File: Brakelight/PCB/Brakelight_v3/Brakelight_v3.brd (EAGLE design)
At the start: 61.1 x 55.9 mm, 57 parts, among them U1 LM358MX

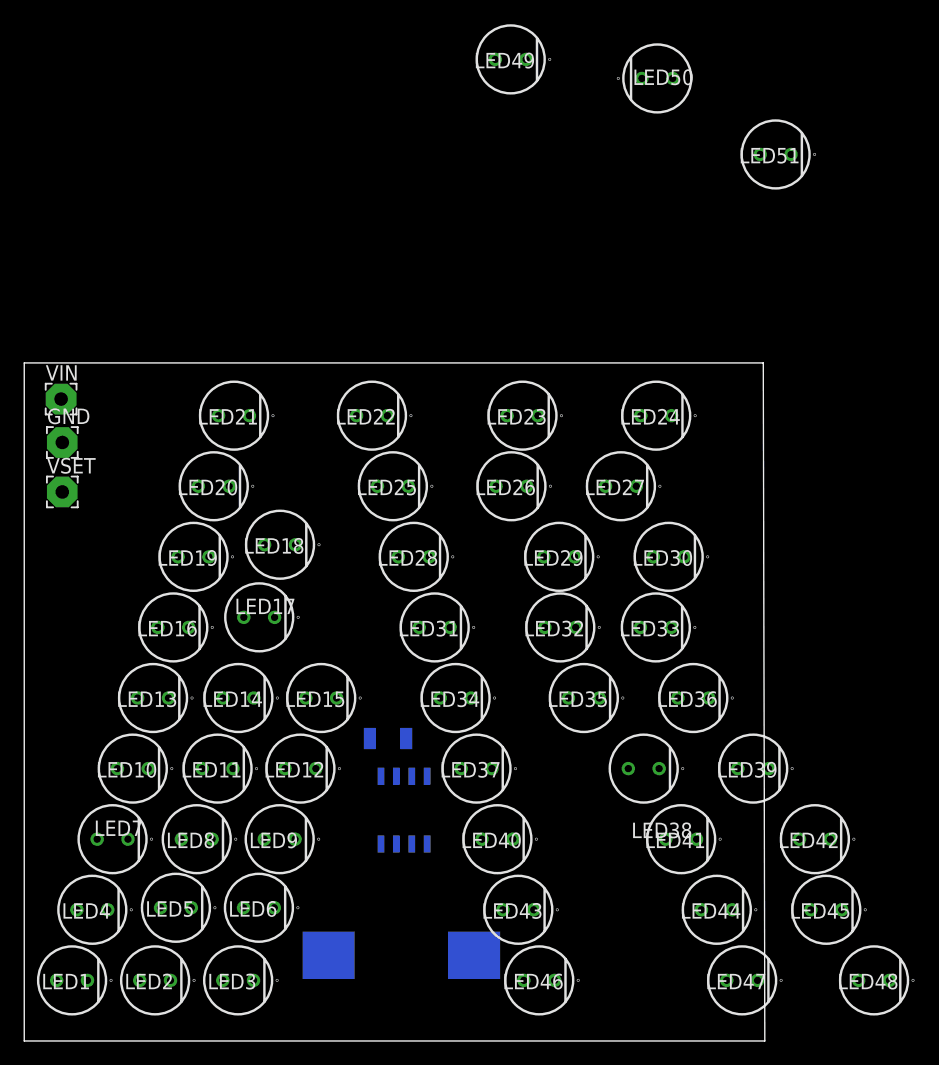
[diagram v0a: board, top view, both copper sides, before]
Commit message: Brakelight - Fixed positions ready for tracing
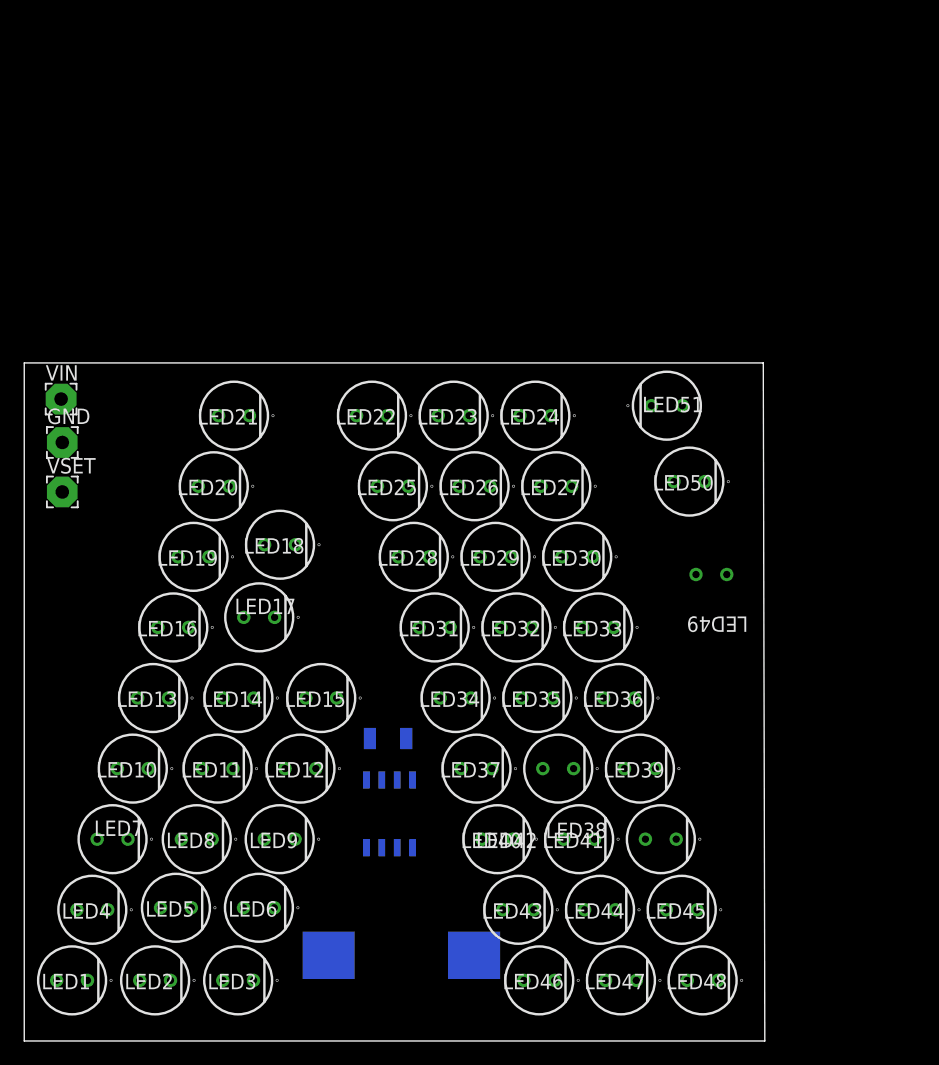
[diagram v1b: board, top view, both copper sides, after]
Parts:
- moved LED49 45.6 mm to (56.5, 36.0), flipped to the bottom
- moved LED50 33.4 mm to (54.7, 43.6), turned to 0 degrees
- moved LED51 22.6 mm to (52.9, 49.9), turned to 180 degrees
- moved LED48 14.1 mm to (55.8, 2.50)
- moved LED42 12.7 mm to (52.4, 14.1)
- moved LED45 11.9 mm to (54.1, 8.32)
- moved LED47 10.00 mm to (49.1, 2.50)
- moved LED24 9.97 mm to (42.0, 49.1)
- moved LED44 9.63 mm to (47.3, 8.32)
- moved LED39 9.34 mm to (50.6, 20.0)
- moved LED41 8.42 mm to (45.6, 14.1)
- moved LED30 7.55 mm to (45.5, 37.4)
- moved LED38 7.05 mm to (43.9, 20.0)
- moved LED36 6.13 mm to (48.9, 25.8)
- moved LED23 5.68 mm to (35.3, 49.1)
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
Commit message: Brakelight only stubs left
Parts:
- moved VIN 40.0 mm to (27.9, 19.2), flipped to the bottom
- moved GND 39.3 mm to (27.9, 16.5), flipped to the bottom
- moved VSET 38.3 mm to (27.9, 13.7), flipped to the bottom
- moved U1 2.16 mm to (32.1, 15.7)
- moved R1 2.00 mm to (31.9, 22.4), turned to 135 degrees
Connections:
- net N$36 renamed LEDK
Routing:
- net LEDK: track 0.00 -> 155.2 mm
- net N$37: track 0.00 -> 19.5 mm
- net N$35: track 0.00 -> 11.3 mm, vias 0 -> 1
- net ISENSE: track 0.00 -> 8.38 mm
- net N$33: track 0.00 -> 7.88 mm
- net N$34: track 0.00 -> 6.53 mm
- net N$12: track 0.00 -> 6.05 mm
- net N$14: track 0.00 -> 5.89 mm
- net N$13: track 0.00 -> 5.89 mm
- net VIN: track 0.00 -> 5.40 mm
- net N$11: track 0.00 -> 4.62 mm
- net N$9: track 0.00 -> 4.50 mm
- net N$7: track 0.00 -> 4.45 mm
- net N$5: track 0.00 -> 4.40 mm
- net N$3: track 0.00 -> 4.36 mm
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- added copper zone on layer 16, net GND
- added copper zone on layer 1, net ISENSE

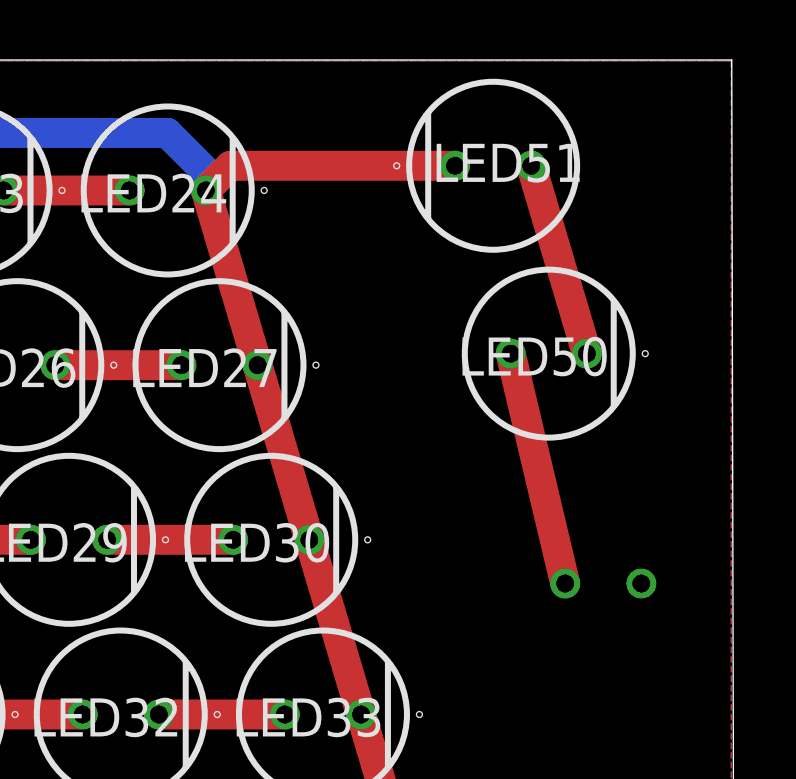
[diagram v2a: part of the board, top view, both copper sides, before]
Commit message: Ready: Brakelight PCB
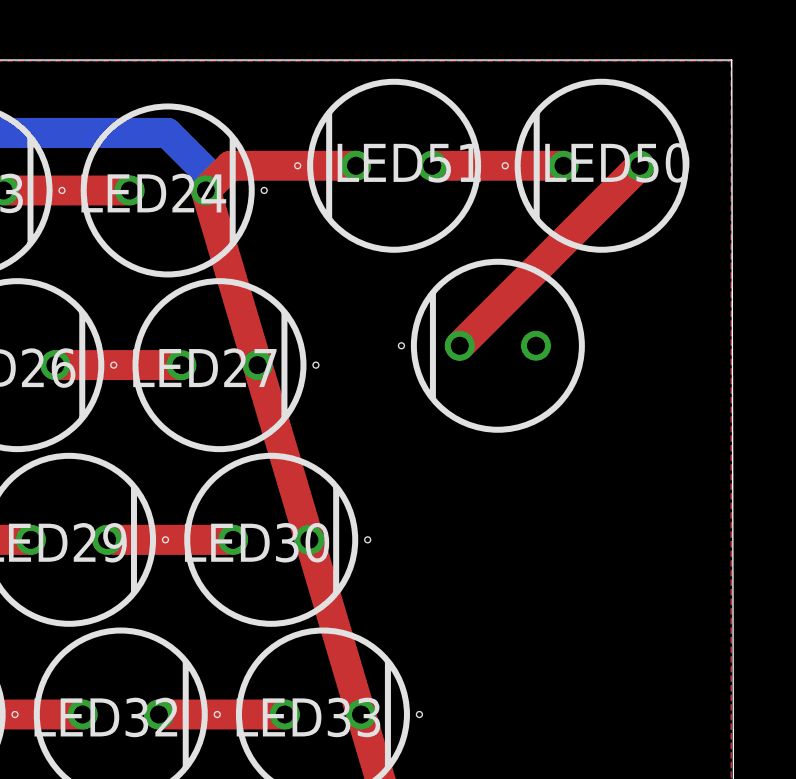
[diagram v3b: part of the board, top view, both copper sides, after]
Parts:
- moved LED49 8.67 mm to (53.0, 43.9), flipped to the top, turned to 180 degrees
- moved LED50 6.50 mm to (56.5, 49.9), turned to 180 degrees
- moved LED51 3.30 mm to (49.6, 49.9)
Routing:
- net LEDK: track 155.2 -> 151.9 mm
- net N$34: track 6.53 -> 4.38 mm
- net N$33: track 7.88 -> 8.48 mm
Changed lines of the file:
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@@
 <?xml version="1.0" encoding="utf-8"?>
 <!DOCTYPE eagle SYSTEM "eagle.dtd">
-<eagle version="9.2.2">
+<eagle version="9.2.1">
 <drawing>
 <settings>
@@
 <attribute name="VALUE" x="55.31395" y="2.403" size="0.4064" layer="27" align="center"/>
 </element>
-<element name="LED49" library="5mm (T-1 34) Round LED" package="SSL-LX5093SGC/B" value="SSL-LX5093TC" x="56.53" y="35.98" smashed="yes" rot="MR0">
-<attribute name="DESCRIPTION" value="Lumex SSL-LX5093TC Turquoise LED, 5mm (T-1 3/4) Clear, Dome Lens Through Hole Package" x="23.51" y="-41.49" size="1.778" layer="28" rot="MR0" display="off"/>
-<attribute name="HEIGHT" value="mm" x="23.51" y="-41.49" size="1.778" layer="28" rot="MR0" display="off"/>
-<attribute name="MANUFACTURER_NAME" value="Lumex" x="23.51" y="-41.49" size="1.778" layer="28" rot="MR0" display="off"/>
-<attribute name="MANUFACTURER_PART_NUMBER" value="SSL-LX5093TC" x="23.51" y="-41.49" size="1.778" layer="28" rot="MR0" display="off"/>
-<attribute name="MOUSER_PART_NUMBER" value="696-SSL-LX5093TC" x="23.51" y="-41.49" size="1.778" layer="28" rot="MR0" display="off"/>
-<attribute name="NAME" x="56.627" y="32.183" size="1.27" layer="27" rot="MR180" align="center"/>
-<attribute name="VALUE" x="57.027" y="37.383" size="0.4064" layer="27" rot="MR180" align="center"/>
+<element name="LED49" library="5mm (T-1 34) Round LED" package="SSL-LX5093SGC/B" value="SSL-LX5093TC" x="53.0176625" y="43.90501875" smashed="yes" rot="R180">
+<attribute name="DESCRIPTION" value="Lumex SSL-LX5093TC Turquoise LED, 5mm (T-1 3/4) Clear, Dome Lens Through Hole Package" x="19.9976625" y="121.37501875" size="1.778" layer="27" rot="R180" display="off"/>
+<attribute name="HEIGHT" value="mm" x="19.9976625" y="121.37501875" size="1.778" layer="27" rot="R180" display="off"/>
+<attribute name="MANUFACTURER_NAME" value="Lumex" x="19.9976625" y="121.37501875" size="1.778" layer="27" rot="R180" display="off"/>
+<attribute name="MANUFACTURER_PART_NUMBER" value="SSL-LX5093TC" x="19.9976625" y="121.37501875" size="1.778" layer="27" rot="R180" display="off"/>
+<attribute name="MOUSER_PART_NUMBER" value="696-SSL-LX5093TC" x="19.9976625" y="121.37501875" size="1.778" layer="27" rot="R180" display="off"/>
+<attribute name="NAME" x="53.1146625" y="41.70201875" size="1.27" layer="27" align="center"/>
+<attribute name="VALUE" x="53.5146625" y="42.50201875" size="0.4064" layer="28" align="center"/>
 </element>
 <element name="LED5" library="5mm (T-1 34) Round LED" package="SSL-LX5093SGC/B" value="SSL-LX5093TC" x="12.362984375" y="8.48914375" smashed="yes">
@@
 <attribute name="VALUE" x="14.865984375" y="9.39214375" size="0.4064" layer="27" align="center"/>
 </element>
-<element name="LED50" library="5mm (T-1 34) Round LED" package="SSL-LX5093SGC/B" value="SSL-LX5093TC" x="54.7144125" y="43.643396875" smashed="yes">
-<attribute name="DESCRIPTION" value="Lumex SSL-LX5093TC Turquoise LED, 5mm (T-1 3/4) Clear, Dome Lens Through Hole Package" x="101.7044125" y="-33.826603125" size="1.778" layer="27" display="off"/>
-<attribute name="HEIGHT" value="mm" x="101.7044125" y="-33.826603125" size="1.778" layer="27" display="off"/>
-<attribute name="MANUFACTURER_NAME" value="Lumex" x="101.7044125" y="-33.826603125" size="1.778" layer="27" display="off"/>
-<attribute name="MANUFACTURER_PART_NUMBER" value="SSL-LX5093TC" x="101.7044125" y="-33.826603125" size="1.778" layer="27" display="off"/>
-<attribute name="MOUSER_PART_NUMBER" value="696-SSL-LX5093TC" x="101.7044125" y="-33.826603125" size="1.778" layer="27" display="off"/>
-<attribute name="NAME" x="54.2174125" y="43.546396875" size="1.27" layer="25" align="center"/>
-<attribute name="VALUE" x="52.2174125" y="40.546396875" size="0.4064" layer="27" align="center"/>
-</element>
-<element name="LED51" library="5mm (T-1 34) Round LED" package="SSL-LX5093SGC/B" value="SSL-LX5093TC" x="52.85920625" y="49.90501875" smashed="yes" rot="R180">
-<attribute name="DESCRIPTION" value="Lumex SSL-LX5093TC Turquoise LED, 5mm (T-1 3/4) Clear, Dome Lens Through Hole Package" x="-8.10079375" y="127.37501875" size="1.778" layer="27" rot="R180" display="off"/>
-<attribute name="HEIGHT" value="mm" x="-8.10079375" y="127.37501875" size="1.778" layer="27" rot="R180" display="off"/>
-<attribute name="MANUFACTURER_NAME" value="Lumex" x="-8.10079375" y="127.37501875" size="1.778" layer="27" rot="R180" display="off"/>
-<attribute name="MANUFACTURER_PART_NUMBER" value="SSL-LX5093TC" x="-8.10079375" y="127.37501875" size="1.778" layer="27" rot="R180" display="off"/>
-<attribute name="MOUSER_PART_NUMBER" value="696-SSL-LX5093TC" x="-8.10079375" y="127.37501875" size="1.778" layer="27" rot="R180" display="off"/>
-<attribute name="NAME" x="53.35620625" y="50.00201875" size="1.27" layer="25" rot="R180" align="center"/>
-<attribute name="VALUE" x="52.08620625" y="43.65201875" size="0.4064" layer="27" rot="R180" align="center"/>
+<element name="LED50" library="5mm (T-1 34) Round LED" package="SSL-LX5093SGC/B" value="SSL-LX5093TC" x="56.4766" y="49.90501875" smashed="yes" rot="R180">
+<attribute name="DESCRIPTION" value="Lumex SSL-LX5093TC Turquoise LED, 5mm (T-1 3/4) Clear, Dome Lens Through Hole Package" x="9.4866" y="127.37501875" size="1.778" layer="27" rot="R180" display="off"/>
+<attribute name="HEIGHT" value="mm" x="9.4866" y="127.37501875" size="1.778" layer="27" rot="R180" display="off"/>
+<attribute name="MANUFACTURER_NAME" value="Lumex" x="9.4866" y="127.37501875" size="1.778" layer="27" rot="R180" display="off"/>
+<attribute name="MANUFACTURER_PART_NUMBER" value="SSL-LX5093TC" x="9.4866" y="127.37501875" size="1.778" layer="27" rot="R180" display="off"/>
+<attribute name="MOUSER_PART_NUMBER" value="696-SSL-LX5093TC" x="9.4866" y="127.37501875" size="1.778" layer="27" rot="R180" display="off"/>
+<attribute name="NAME" x="56.9736" y="50.00201875" size="1.27" layer="25" rot="R180" align="center"/>
+<attribute name="VALUE" x="58.9736" y="53.00201875" size="0.4064" layer="27" rot="R180" align="center"/>
+</element>
+<element name="LED51" library="5mm (T-1 34) Round LED" package="SSL-LX5093SGC/B" value="SSL-LX5093TC" x="49.558728125" y="49.90501875" smashed="yes" rot="R180">
+<attribute name="DESCRIPTION" value="Lumex SSL-LX5093TC Turquoise LED, 5mm (T-1 3/4) Clear, Dome Lens Through Hole Package" x="-11.401271875" y="127.37501875" size="1.778" layer="27" rot="R180" display="off"/>
+<attribute name="HEIGHT" value="mm" x="-11.401271875" y="127.37501875" size="1.778" layer="27" rot="R180" display="off"/>
+<attribute name="MANUFACTURER_NAME" value="Lumex" x="-11.401271875" y="127.37501875" size="1.778" layer="27" rot="R180" display="off"/>
+<attribute name="MANUFACTURER_PART_NUMBER" value="SSL-LX5093TC" x="-11.401271875" y="127.37501875" size="1.778" layer="27" rot="R180" display="off"/>
+<attribute name="MOUSER_PART_NUMBER" value="696-SSL-LX5093TC" x="-11.401271875" y="127.37501875" size="1.778" layer="27" rot="R180" display="off"/>
+<attribute name="NAME" x="50.055728125" y="50.00201875" size="1.27" layer="25" rot="R180" align="center"/>
+<attribute name="VALUE" x="48.785728125" y="43.65201875" size="0.4064" layer="27" rot="R180" align="center"/>
 </element>
 <element name="LED6" library="5mm (T-1 34) Round LED" package="SSL-LX5093SGC/B" value="SSL-LX5093TC" x="19.20794375" y="8.48914375" smashed="yes">
@@
 <contactref element="LED50" pad="2"/>
 <contactref element="LED49" pad="1"/>
-<wire x1="53.4444125" y1="43.643396875" x2="55.26" y2="35.98" width="1" layer="1"/>
+<wire x1="57.7466" y1="49.90501875" x2="51.7476625" y2="43.90501875" width="1" layer="1"/>
 </signal>
 <signal name="N$34">
 <contactref element="LED50" pad="1"/>
 <contactref element="LED51" pad="2"/>
-<wire x1="54.12920625" y1="49.90501875" x2="55.9844125" y2="43.643396875" width="1" layer="1"/>
+<wire x1="50.828728125" y1="49.90501875" x2="55.2066" y2="49.90501875" width="1" layer="1"/>
 </signal>
 <signal name="ISENSE">
@@
 <wire x1="22.1910125" y1="14.145559375" x2="24.96" y2="4.58" width="1" layer="16"/>
 <wire x1="55.356165625" y1="8.32278125" x2="57.08095" y2="2.5" width="1" layer="1"/>
-<wire x1="51.58920625" y1="49.90501875" x2="44.105440625" y2="49.90501875" width="1" layer="1"/>
-<wire x1="44.105440625" y1="49.90501875" x2="43.2826625" y2="49.082240625" width="1" layer="1"/>
 <wire x1="43.2826625" y1="49.7173375" x2="43.2826625" y2="49.082240625" width="1" layer="16"/>
 <wire x1="42" y1="51" x2="43.2826625" y2="49.7173375" width="1" layer="16"/>
@@
 <wire x1="20.47794375" y1="8.48914375" x2="24.96" y2="4.58" width="1" layer="16"/>
 <wire x1="18.764878125" y1="2.5" x2="24.96" y2="4.58" width="1" layer="16"/>
+<wire x1="43.2826625" y1="49.082240625" x2="44.105440625" y2="49.90501875" width="1" layer="1"/>
+<wire x1="44.105440625" y1="49.90501875" x2="48.288728125" y2="49.90501875" width="1" layer="1"/>
 </signal>
 <signal name="N$37">
